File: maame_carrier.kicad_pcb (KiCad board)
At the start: 2 copper layers, 130 x 72 mm, 25 parts, among them J1 To Kakute pads: 5V G R3 T4 R4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, J10 FS-iA10B iBUS servo lead (S +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, J11 TF-Luna pin order 1-6 (CFG ti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, J12 Spare FC I2C (5 V supply, sha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, J13 Payload servo on M5 (S + -), J14 Spare output M6 (S + -), J15 Spare output M7 (S + -), J16 Spare output M8 (S + -), J2 To Kakute 8-pin port 2 leads: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, J3 VBAT tap from ESC battery pad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, J4 Micro BEC input leads, J5 Micro BEC output leads (set t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, J6 Spare power: 5V_AUX G 5V_FC G, J7 Pi expansion: 3V3 logic ONLY, J8 TBS M10Q: order matches its p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, J9 SiK radio (UART4), U1 Raspberry Pi Zero W v1.1, com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

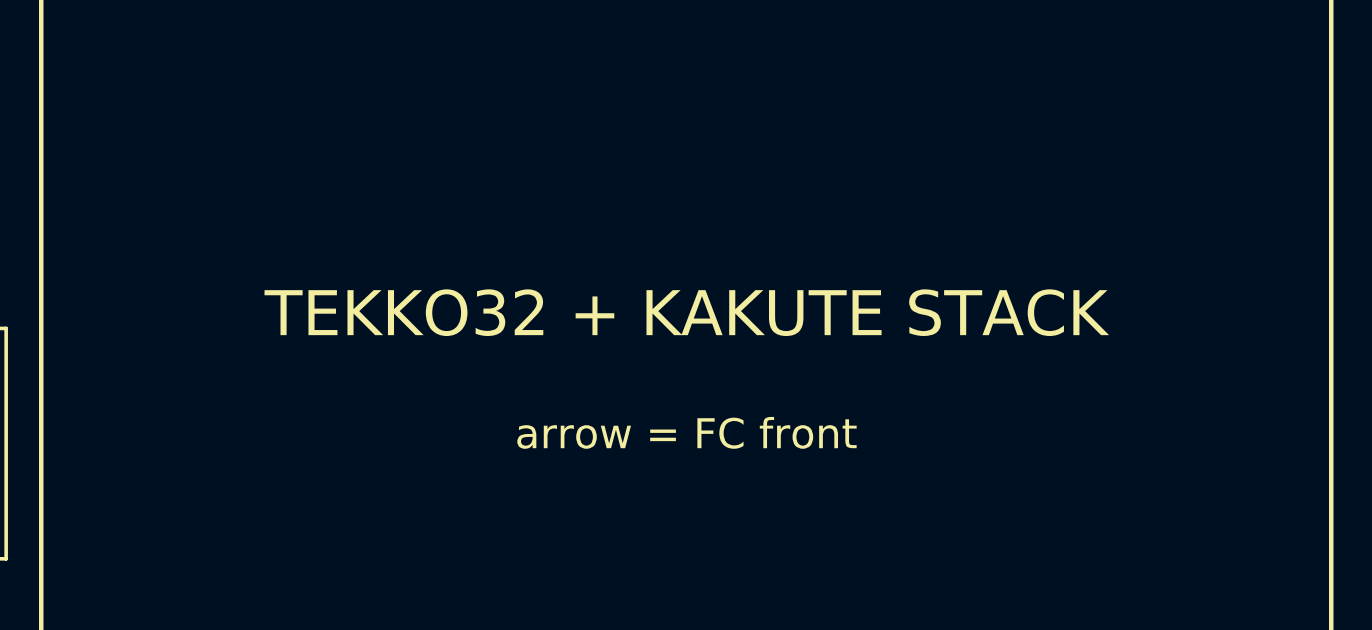
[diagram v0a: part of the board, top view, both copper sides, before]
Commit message: ESC off the carrier: FC-only 35x35 keep-out, relabel, update notes
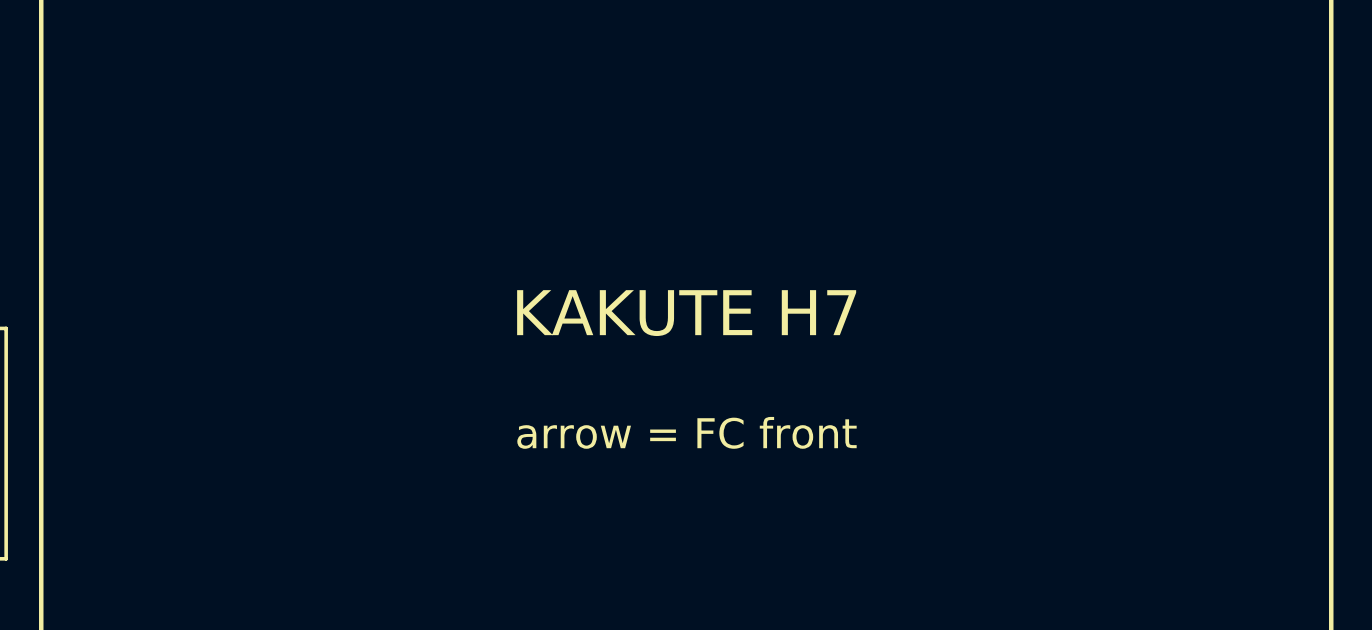
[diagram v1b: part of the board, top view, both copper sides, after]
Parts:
- H1, H2, H3, H4: value M3 stack hole -> M3 FC hole
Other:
- board text added: "KAKUTE H7"
- board text removed: "TEKKO32 + KAKUTE STACK"
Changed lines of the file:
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@@
 			)
 		)
-		(property "Value" "M3 stack hole"
+		(property "Value" "M3 FC hole"
 			(at 0 4.2 0)
 			(layer "F.Fab")
@@
 			)
 		)
-		(property "Value" "M3 stack hole"
+		(property "Value" "M3 FC hole"
 			(at 0 4.2 0)
 			(layer "F.Fab")
@@
 			)
 		)
-		(property "Value" "M3 stack hole"
+		(property "Value" "M3 FC hole"
 			(at 0 4.2 0)
 			(layer "F.Fab")
@@
 			)
 		)
-		(property "Value" "M3 stack hole"
+		(property "Value" "M3 FC hole"
 			(at 0 4.2 0)
 			(layer "F.Fab")
@@
 	)
 	(gr_line
-		(start 8.5 14)
-		(end 51.5 14)
+		(start 12.5 18.5)
+		(end 47.5 18.5)
 		(stroke
 			(width 0.1)
@@
 	)
 	(gr_line
-		(start 8.5 58)
-		(end 8.5 14)
+		(start 12.5 53.5)
+		(end 12.5 18.5)
 		(stroke
 			(width 0.1)
@@
 	)
 	(gr_line
-		(start 51.5 14)
-		(end 51.5 58)
+		(start 47.5 18.5)
+		(end 47.5 53.5)
 		(stroke
 			(width 0.1)
@@
 	)
 	(gr_line
-		(start 51.5 58)
-		(end 8.5 58)
+		(start 47.5 53.5)
+		(end 12.5 53.5)
 		(stroke
 			(width 0.1)
@@
 		)
 	)
-	(gr_text "TEKKO32 + KAKUTE STACK"
+	(gr_text "KAKUTE H7"
 		(at 30 33 0)
 		(layer "F.SilkS")

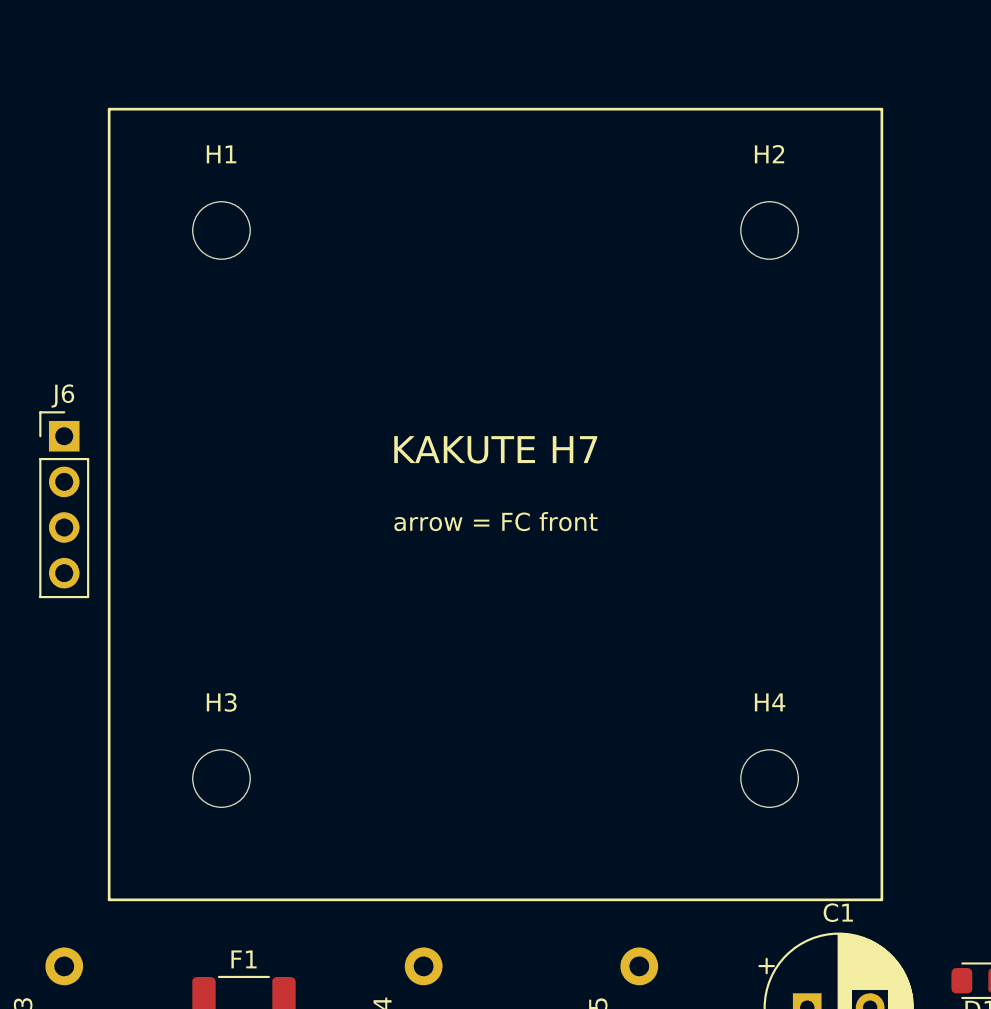
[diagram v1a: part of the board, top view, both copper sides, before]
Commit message: Add 14x5 mm ESC cable slot at FC centre; shrink FC silk box to 35x35
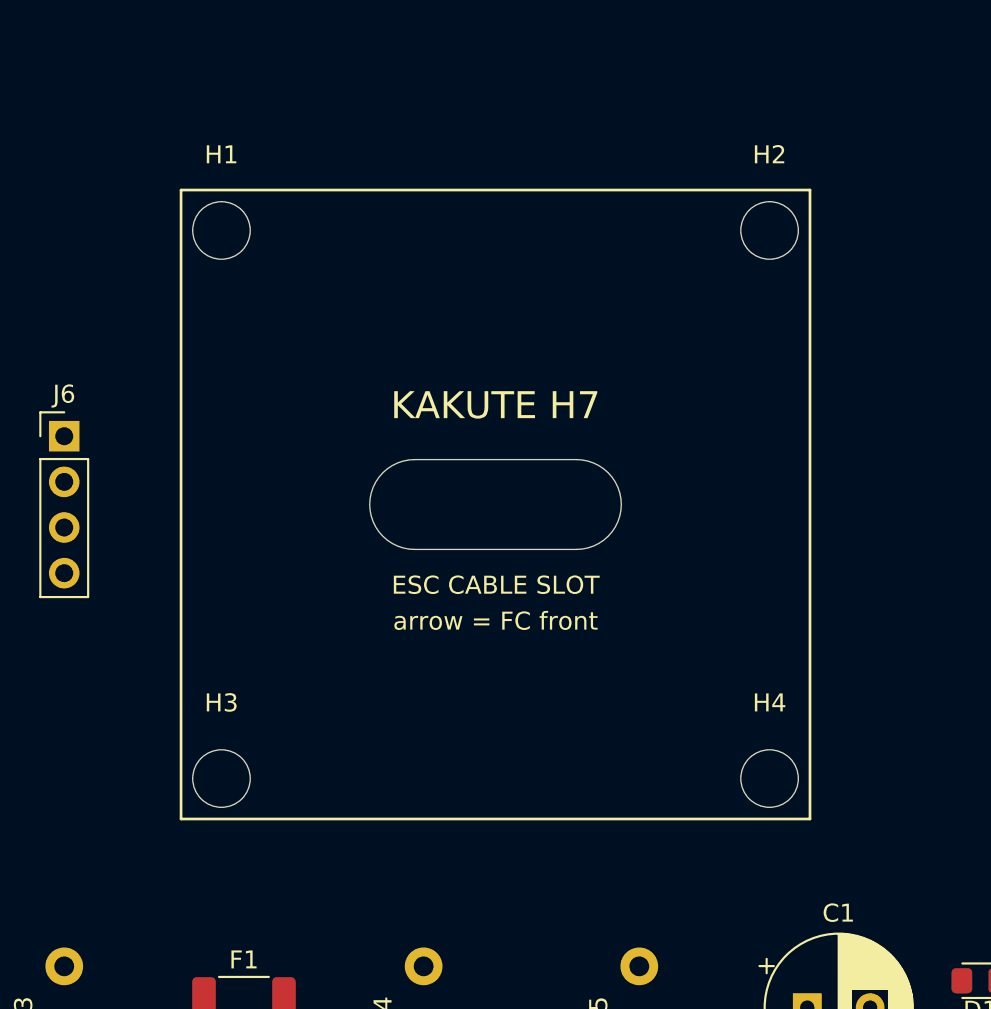
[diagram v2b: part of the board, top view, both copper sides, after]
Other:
- outline, holes or cut-outs redrawn
- board text added: "ESC CABLE SLOT"
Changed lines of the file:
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@@
 	)
 	(gr_line
-		(start 8.5 14)
-		(end 51.5 14)
+		(start 12.5 18.5)
+		(end 47.5 18.5)
 		(stroke
 			(width 0.15)
@@
 	)
 	(gr_line
-		(start 8.5 58)
-		(end 8.5 14)
+		(start 12.5 53.5)
+		(end 12.5 18.5)
 		(stroke
 			(width 0.15)
@@
 	)
 	(gr_line
-		(start 51.5 14)
-		(end 51.5 58)
+		(start 47.5 18.5)
+		(end 47.5 53.5)
 		(stroke
 			(width 0.15)
@@
 	)
 	(gr_line
-		(start 51.5 58)
-		(end 8.5 58)
+		(start 47.5 53.5)
+		(end 12.5 53.5)
 		(stroke
 			(width 0.15)
@@
 	)
 	(gr_text "arrow = FC front"
-		(at 30 37 0)
+		(at 30 42.5 0)
 		(layer "F.SilkS")
 		(effects
@@
 	)
 	(gr_text "KAKUTE H7"
-		(at 30 33 0)
+		(at 30 30.5 0)
 		(layer "F.SilkS")
 		(effects
@@
 			)
 		)
+	)
+	(gr_line
+		(start 25.5 33.5)
+		(end 34.5 33.5)
+		(stroke
+			(width 0.05)
+			(type default)
+		)
+		(layer "Edge.Cuts")
+	)
+	(gr_arc
+		(start 34.5 33.5)
+		(mid 37 36)
+		(end 34.5 38.5)
+		(stroke
+			(width 0.05)
+			(type default)
+		)
+		(layer "Edge.Cuts")
+	)
+	(gr_line
+		(start 34.5 38.5)
+		(end 25.5 38.5)
+		(stroke
+			(width 0.05)
+			(type default)
+		)
+		(layer "Edge.Cuts")
+	)
+	(gr_arc
+		(start 25.5 38.5)
+		(mid 23 36)
+		(end 25.5 33.5)
+		(stroke
+			(width 0.05)
+			(type default)
+		)
+		(layer "Edge.Cuts")
+	)
+	(gr_text "ESC CABLE SLOT"
+		(at 30 40.5 0)
+		(layer "F.SilkS")
+		(effects
+			(font
+				(size 1 1)
+				(thickness 0.15)
+			)
+		)

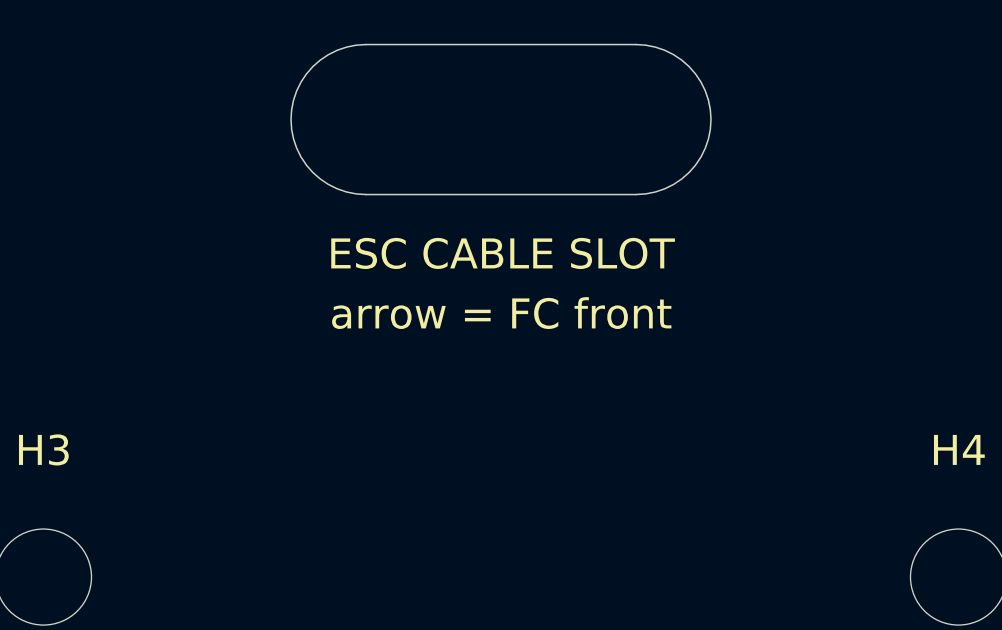
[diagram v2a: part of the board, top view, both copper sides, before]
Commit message: Front is set by the Kakute's own arrow; drop the undrawn carrier arrow note
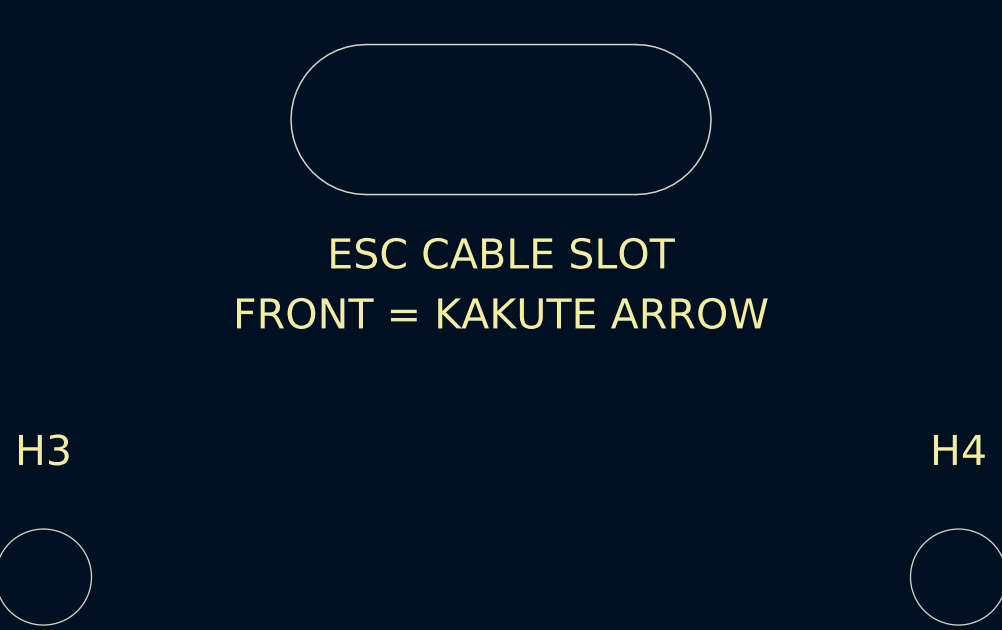
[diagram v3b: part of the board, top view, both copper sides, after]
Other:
- board text added: "FRONT = KAKUTE ARROW"
- board text removed: "arrow = FC front"
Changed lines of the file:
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@@
 		)
 	)
-	(gr_text "arrow = FC front"
+	(gr_text "FRONT = KAKUTE ARROW"
 		(at 30 42.5 0)
 		(layer "F.SilkS")

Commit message: Kakute pad rows follow the V1.5 pad map: 9 pads by its left strip, T1/R1/G by its JST, J2 by port 2; per-pin labels
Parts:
- J1: value To Kakute pads: 5V G R3 T4 R4 T6 R6 SDA -> To Kakute: left strip R3 G 5V R4 T4 SDA SCL R6 T6, JST T1 R1 G; footprint Connector_PinHeader_2.54mm:PinHeader_1x12_P2.54mm_Vertical -> maame_carrier:Kakute_Pads_L9_R3
- moved J6 54.8 mm to (59.0, 46.0)
- moved J1 50.1 mm to (9.00, 25.8)
- moved J2 32.8 mm to (51.0, 25.8), turned to 0 degrees
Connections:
- J1 pad 1: 5V_FC -> RC_IBUS
- J1 pad 3: RC_IBUS -> 5V_FC
- J1 pad 4: UART4_FC_TX -> UART4_FC_RX
- J1 pad 5: UART4_FC_RX -> UART4_FC_TX
- J1 pad 6: UART6_FC_TX -> I2C_SDA
- J1 pad 7: UART6_FC_RX -> I2C_SCL
- J1 pad 8: I2C_SDA -> UART6_FC_RX
- J1 pad 9: I2C_SCL -> UART6_FC_TX
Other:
- board text added: "G"
- board text added: "M5"
- board text added: "M6"
- board text added: "M7"
- board text added: "M8"

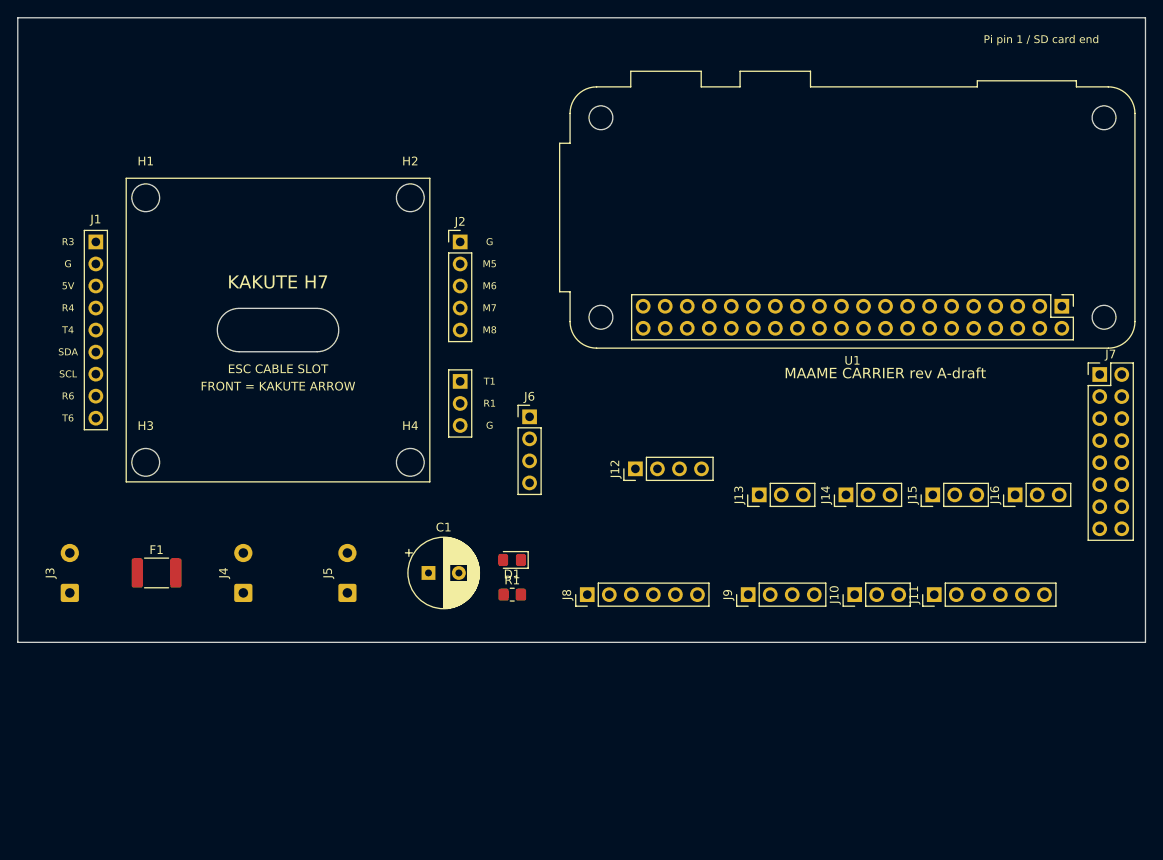
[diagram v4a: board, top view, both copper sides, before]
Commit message: Compact placement into 95x95 placeholder: Kakute group top-left, power row, Pi along bottom edge, headers right
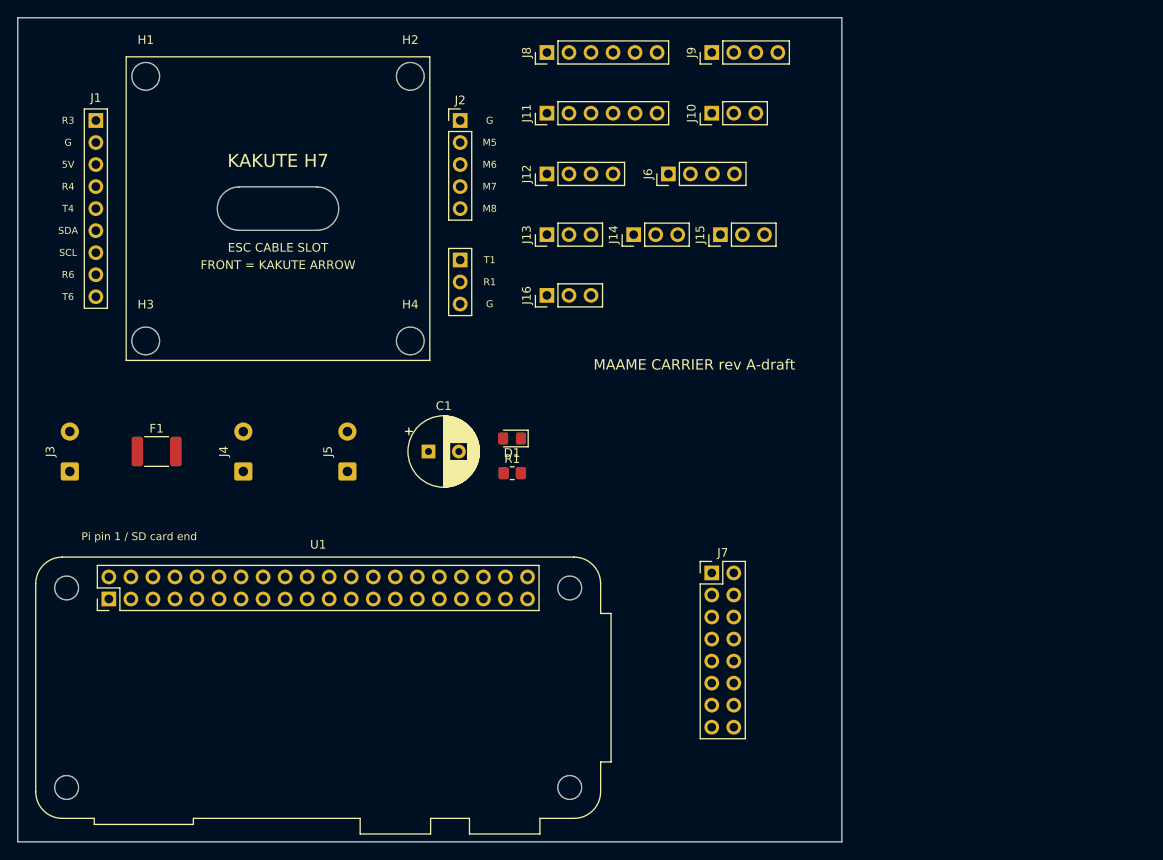
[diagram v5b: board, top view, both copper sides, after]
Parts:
- moved U1 114.9 mm to (10.5, 67.0), turned to 270 degrees
- moved J11 71.2 mm to (61.0, 11.0)
- moved J8 62.7 mm to (61.0, 4.00)
- moved J9 62.6 mm to (80.0, 4.00)
- moved J16 58.7 mm to (61.0, 32.0)
- moved J10 57.9 mm to (80.0, 11.0)
- moved J7 50.2 mm to (80.0, 64.0)
- moved J13 38.7 mm to (61.0, 25.0)
- moved J14 38.7 mm to (71.0, 25.0)
- moved J15 38.7 mm to (81.0, 25.0)
- moved J12 35.5 mm to (61.0, 18.0)
- moved J6 32.2 mm to (75.0, 18.0), turned to 90 degrees
- moved C1 14.0 mm to (47.3, 50.0)
- moved D1 14.0 mm to (57.0, 48.5)
- moved F1 14.0 mm to (16.0, 50.0)
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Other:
- board size 130 x 72 mm -> 95 x 95 mm
